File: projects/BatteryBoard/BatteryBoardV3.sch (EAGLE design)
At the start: 231 parts, among them M1 BSO201SP, SW1 BTS50015-1TAD, SW2 BTS50015-1TAD, T1 AD590FLATPACK, T2 AD590FLATPACK, T3 AD590FLATPACK, T4 AD590FLATPACK, U1 TCA9535PWR, U10 LT1962-3, U11 LT1962-3, U12 LTC4411, U13 LTC4411, U14 LTC4121, U16 LTC4121, U18 AD8418, U19 AD8418, U2 AD7991-0, U3 LTC4412MPS6, U4 LTC4121-4.2, U5 LTC4121-4.2, U6 LC05111C13MTTTG, U7 LC05111C13MTTTG, U8 AD8418, U9 AD8418

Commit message: Completed layout
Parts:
- R41, R59: device BrownSpaceEngineering:RES1210 -> BrownSpaceEngineering:RES
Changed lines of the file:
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@@
 <?xml version="1.0" encoding="utf-8"?>
 <!DOCTYPE eagle SYSTEM "eagle.dtd">
-<eagle version="8.4.0">
+<eagle version="8.2.2">
 <drawing>
 <settings>
 <setting alwaysvectorfont="no"/>
-<setting keepoldvectorfont="yes"/>
 <setting verticaltext="up"/>
 </settings>
 <grid distance="0.1" unitdist="inch" unit="inch" style="lines" multiple="1" display="no" altdistance="0.01" altunitdist="inch" altunit="inch"/>
 <layers>
-<layer number="1" name="Top" color="4" fill="1" visible="no" active="no"/>
-<layer number="2" name="Route2" color="1" fill="3" visible="no" active="no"/>
-<layer number="3" name="Route3" color="4" fill="3" visible="no" active="no"/>
-<layer number="4" name="Route4" color="1" fill="4" visible="no" active="no"/>
-<layer number="5" name="Route5" color="4" fill="4" visible="no" active="no"/>
-<layer number="6" name="Route6" color="1" fill="8" visible="no" active="no"/>
-<layer number="7" name="Route7" color="4" fill="8" visible="no" active="no"/>
-<layer number="8" name="Route8" color="1" fill="2" visible="no" active="no"/>
-<layer number="9" name="Route9" color="4" fill="2" visible="no" active="no"/>
-<layer number="10" name="Route10" color="1" fill="7" visible="no" active="no"/>
-<layer number="11" name="Route11" color="4" fill="7" visible="no" active="no"/>
-<layer number="12" name="Route12" color="1" fill="5" visible="no" active="no"/>
-<layer number="13" name="Route13" color="4" fill="5" visible="no" active="no"/>
-<layer number="14" name="Route14" color="1" fill="6" visible="no" active="no"/>
-<layer number="15" name="Route15" color="4" fill="6" visible="no" active="no"/>
-<layer number="16" name="Bottom" color="1" fill="1" visible="no" active="no"/>
-<layer number="17" name="Pads" color="2" fill="1" visible="no" active="no"/>
-<layer number="18" name="Vias" color="2" fill="1" visible="no" active="no"/>
-<layer number="19" name="Unrouted" color="6" fill="1" visible="no" active="no"/>
-<layer number="20" name="Dimension" color="15" fill="1" visible="no" active="no"/>
-<layer number="21" name="tPlace" color="7" fill="1" visible="no" active="no"/>
-<layer number="22" name="bPlace" color="7" fill="1" visible="no" active="no"/>
-<layer number="23" name="tOrigins" color="15" fill="1" visible="no" active="no"/>
-<layer number="24" name="bOrigins" color="15" fill="1" visible="no" active="no"/>
-<layer number="25" name="tNames" color="7" fill="1" visible="no" active="no"/>
-<layer number="26" name="bNames" color="7" fill="1" visible="no" active="no"/>
-<layer number="27" name="tValues" color="7" fill="1" visible="no" active="no"/>
-<layer number="28" name="bValues" color="7" fill="1" visible="no" active="no"/>
+<layer number="1" name="Top" color="4" fill="1" visible="yes" active="no"/>
+<layer number="2" name="Route2" color="1" fill="3" visible="yes" active="no"/>
+<layer number="3" name="Route3" color="4" fill="3" visible="yes" active="no"/>
+<layer number="4" name="Route4" color="1" fill="4" visible="yes" active="no"/>
+<layer number="5" name="Route5" color="4" fill="4" visible="yes" active="no"/>
+<layer number="6" name="Route6" color="1" fill="8" visible="yes" active="no"/>
+<layer number="7" name="Route7" color="4" fill="8" visible="yes" active="no"/>
+<layer number="8" name="Route8" color="1" fill="2" visible="yes" active="no"/>
+<layer number="9" name="Route9" color="4" fill="2" visible="yes" active="no"/>
+<layer number="10" name="Route10" color="1" fill="7" visible="yes" active="no"/>
+<layer number="11" name="Route11" color="4" fill="7" visible="yes" active="no"/>
+<layer number="12" name="Route12" color="1" fill="5" visible="yes" active="no"/>
+<layer number="13" name="Route13" color="4" fill="5" visible="yes" active="no"/>
+<layer number="14" name="Route14" color="1" fill="6" visible="yes" active="no"/>
+<layer number="15" name="Route15" color="4" fill="6" visible="yes" active="no"/>
+<layer number="16" name="Bottom" color="1" fill="1" visible="yes" active="no"/>
+<layer number="17" name="Pads" color="2" fill="1" visible="yes" active="no"/>
+<layer number="18" name="Vias" color="2" fill="1" visible="yes" active="no"/>
+<layer number="19" name="Unrouted" color="6" fill="1" visible="yes" active="no"/>
+<layer number="20" name="Dimension" color="15" fill="1" visible="yes" active="no"/>
+<layer number="21" name="tPlace" color="7" fill="1" visible="yes" active="no"/>
+<layer number="22" name="bPlace" color="7" fill="1" visible="yes" active="no"/>
+<layer number="23" name="tOrigins" color="15" fill="1" visible="yes" active="no"/>
+<layer number="24" name="bOrigins" color="15" fill="1" visible="yes" active="no"/>
+<layer number="25" name="tNames" color="7" fill="1" visible="yes" active="no"/>
+<layer number="26" name="bNames" color="7" fill="1" visible="yes" active="no"/>
+<layer number="27" name="tValues" color="7" fill="1" visible="yes" active="no"/>
+<layer number="28" name="bValues" color="7" fill="1" visible="yes" active="no"/>
 <layer number="29" name="tStop" color="7" fill="3" visible="no" active="no"/>
 <layer number="30" name="bStop" color="7" fill="6" visible="no" active="no"/>
@@
 <layer number="35" name="tGlue" color="7" fill="4" visible="no" active="no"/>
 <layer number="36" name="bGlue" color="7" fill="5" visible="no" active="no"/>
-<layer number="37" name="tTest" color="7" fill="1" visible="no" active="no"/>
-<layer number="38" name="bTest" color="7" fill="1" visible="no" active="no"/>
+<layer number="37" name="tTest" color="7" fill="1" visible="yes" active="no"/>
+<layer number="38" name="bTest" color="7" fill="1" visible="yes" active="no"/>
 <layer number="39" name="tKeepout" color="4" fill="11" visible="no" active="no"/>
 <layer number="40" name="bKeepout" color="1" fill="11" visible="no" active="no"/>
@@
 <layer number="44" name="Drills" color="7" fill="1" visible="no" active="no"/>
 <layer number="45" name="Holes" color="7" fill="1" visible="no" active="no"/>
-<layer number="46" name="Milling" color="3" fill="1" visible="no" active="no"/>
-<layer number="47" name="Measures" color="7" fill="1" visible="no" active="no"/>
-<layer number="48" name="Document" color="7" fill="1" visible="no" active="no"/>
-<layer number="49" name="Reference" color="7" fill="1" visible="no" active="no"/>
-<layer number="50" name="dxf" color="7" fill="1" visible="no" active="no"/>
-<layer number="51" name="tDocu" color="7" fill="1" visible="no" active="no"/>
-<layer number="52" name="bDocu" color="7" fill="1" visible="no" active="no"/>
-<layer number="53" name="tGND_GNDA" color="7" fill="9" visible="no" active="no"/>
-<layer number="54" name="bGND_GNDA" color="1" fill="9" visible="no" active="no"/>
-<layer number="56" name="wert" color="7" fill="1" visible="no" active="no"/>
-<layer number="57" name="tCAD" color="7" fill="1" visible="no" active="no"/>
-<layer number="59" name="tCarbon" color="7" fill="1" visible="no" active="no"/>
-<layer number="60" name="bCarbon" color="7" fill="1" visible="no" active="no"/>
+<layer number="46" name="Milling" color="3" fill="1" visible="yes" active="no"/>
+<layer number="47" name="Measures" color="7" fill="1" visible="yes" active="no"/>
+<layer number="48" name="Document" color="7" fill="1" visible="yes" active="no"/>
+<layer number="49" name="Reference" color="7" fill="1" visible="yes" active="no"/>
+<layer number="50" name="dxf" color="7" fill="1" visible="yes" active="no"/>
+<layer number="51" name="tDocu" color="7" fill="1" visible="yes" active="no"/>
+<layer number="52" name="bDocu" color="7" fill="1" visible="yes" active="no"/>
+<layer number="53" name="tGND_GNDA" color="7" fill="9" visible="yes" active="no"/>
+<layer number="54" name="bGND_GNDA" color="1" fill="9" visible="yes" active="no"/>
+<layer number="56" name="wert" color="7" fill="1" visible="yes" active="no"/>
+<layer number="57" name="tCAD" color="7" fill="1" visible="yes" active="no"/>
+<layer number="59" name="tCarbon" color="7" fill="1" visible="yes" active="no"/>
+<layer number="60" name="bCarbon" color="7" fill="1" visible="yes" active="no"/>
 <layer number="90" name="Modules" color="5" fill="1" visible="yes" active="yes"/>
 <layer number="91" name="Nets" color="2" fill="1" visible="yes" active="yes"/>
@@
 <part name="LIFEPO41" library="BrownSpaceEngineering" deviceset="LIFEPO4" device="VA" value="~3.5V"/>
 <part name="LIFEPO42" library="BrownSpaceEngineering" deviceset="LIFEPO4" device="VB" value="~3.5V"/>
-<part name="R41" library="BrownSpaceEngineering" deviceset="RES" device="1210" value="0.001R@3W"/>
+<part name="R41" library="BrownSpaceEngineering" deviceset="RES" device="" value="0.001R@3W"/>
 <part name="GND32" library="supply1" deviceset="GND" device=""/>
 <part name="GND36" library="supply1" deviceset="GND" device=""/>
@@
 <part name="LIFEPO43" library="BrownSpaceEngineering" deviceset="LIFEPO4" device="VA" value="~3.5V"/>
 <part name="LIFEPO44" library="BrownSpaceEngineering" deviceset="LIFEPO4" device="VB" value="~3.5V"/>
-<part name="R59" library="BrownSpaceEngineering" deviceset="RES" device="1210" value="0.001R@3W"/>
+<part name="R59" library="BrownSpaceEngineering" deviceset="RES" device="" value="0.001R@3W"/>
 <part name="GND39" library="supply1" deviceset="GND" device=""/>
 <part name="GND43" library="supply1" deviceset="GND" device=""/>

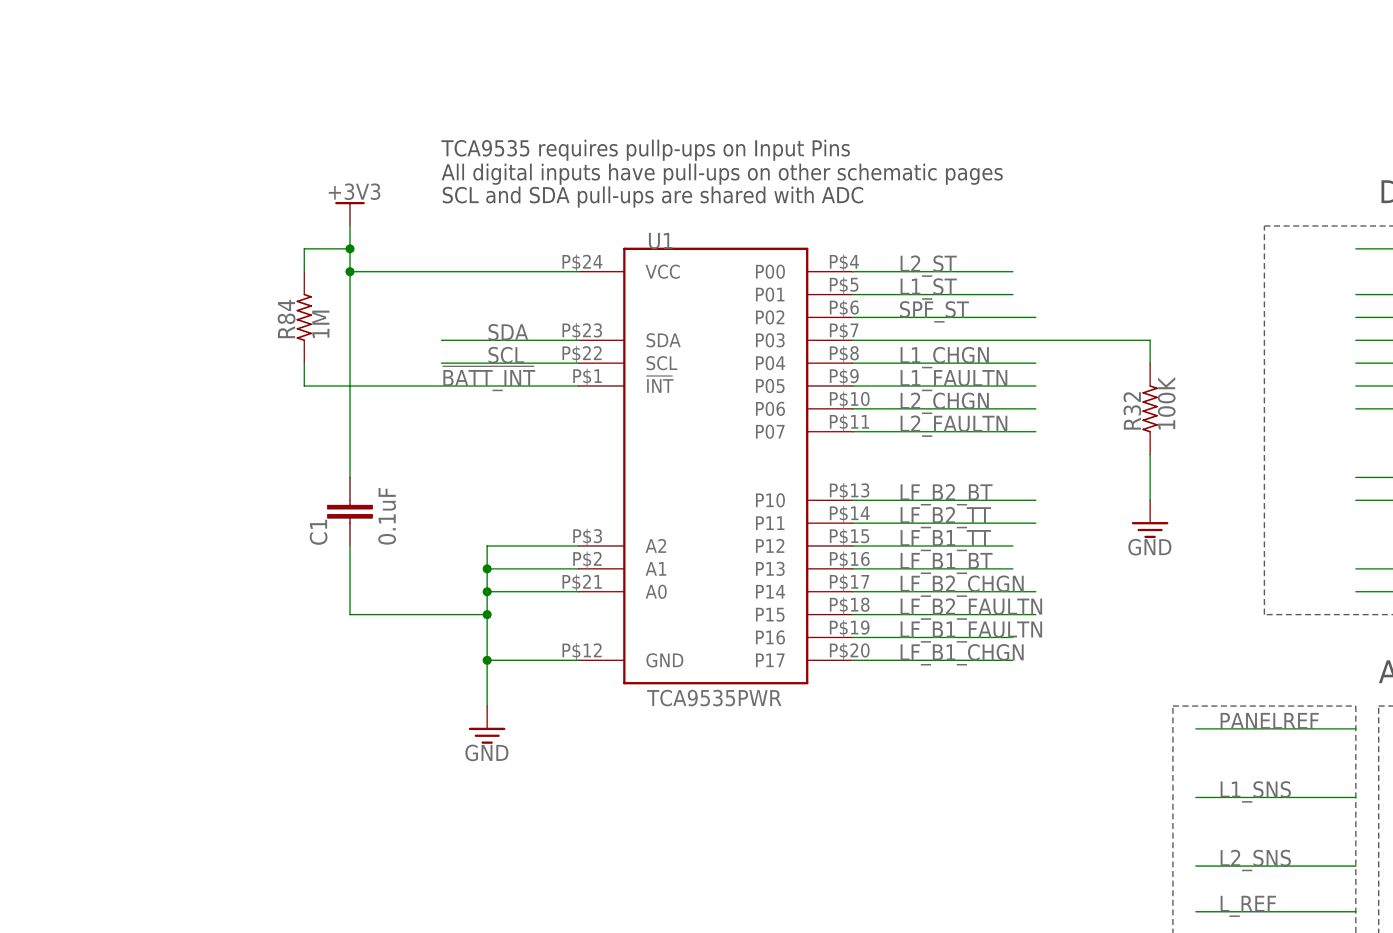
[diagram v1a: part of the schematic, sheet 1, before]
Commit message: 100K pulldowns for unused GPIO expander pins
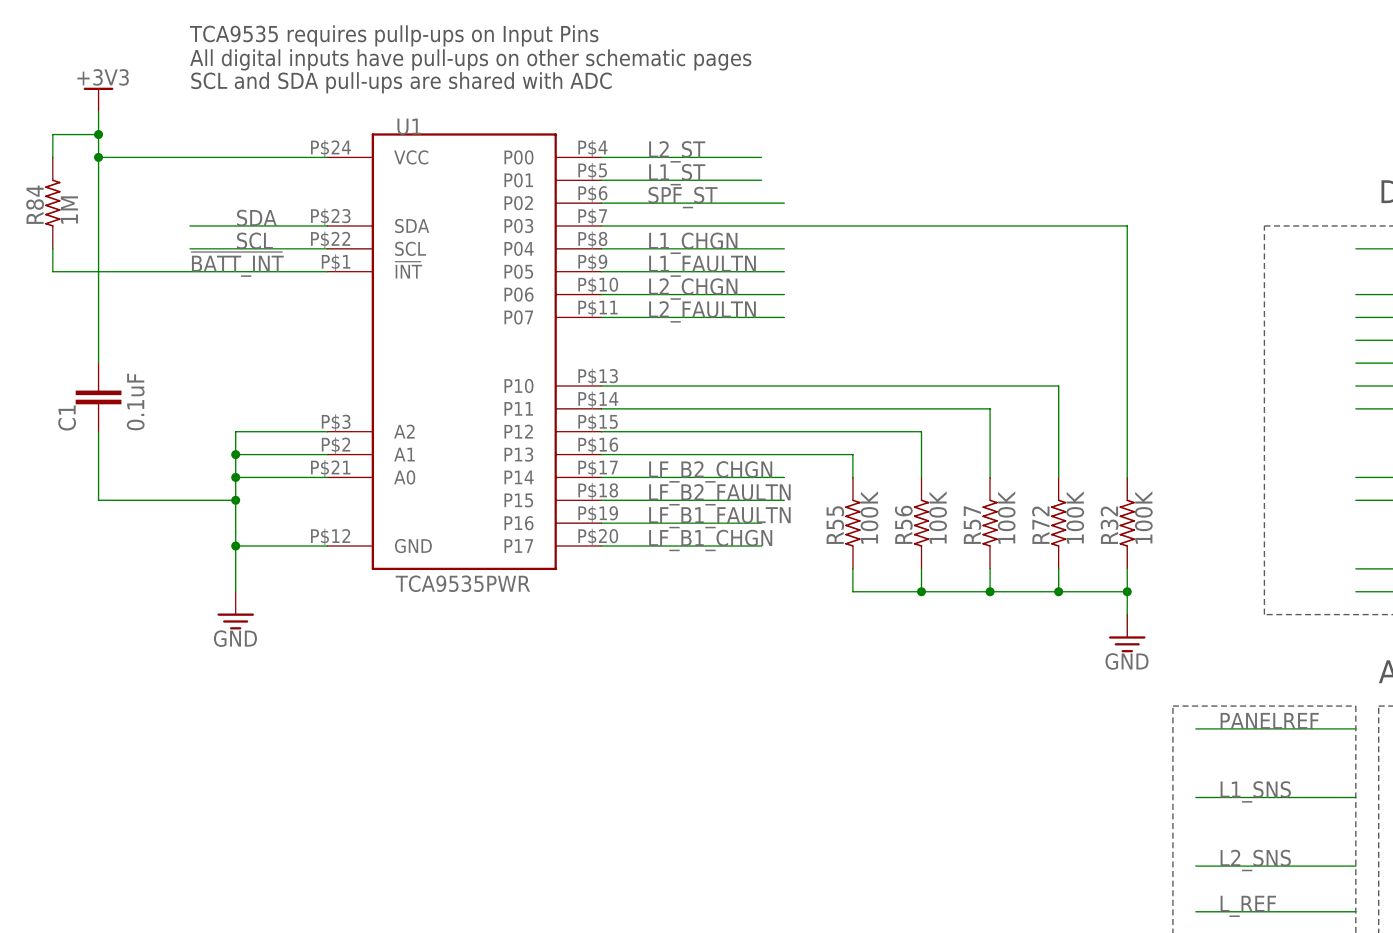
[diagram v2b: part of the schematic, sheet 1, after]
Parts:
- added R55, R56, R57, R72: 100K, BrownSpaceEngineering:RES0805
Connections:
- removed net LF_B1_BT: U1.P13
- removed net LF_B1_TT: U1.P12
- removed net LF_B2_BT: U1.P10
- removed net LF_B2_TT: U1.P11
- new net N$20: R72.2, U1.P10
- new net N$21: R57.2, U1.P11
- new net N$23: R56.2, U1.P12
- new net N$24: R55.2, U1.P13
- net GND: now also R55.1, R56.1, R57.1, R72.1
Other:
- moved on the sheet: C1, R32, R84, U1
